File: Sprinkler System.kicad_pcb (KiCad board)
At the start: 2 copper layers, 165 x 85 mm, 81 parts, among them J1 Main Supply, J2 XFMR_Out, J20 Station_0, J21 Station_1, J22 Station_2, J23 Station_3, J24 Station_4, J25 Station_5, J3 XFMR_In, J4 Conn_Button, J5 UART0, J6 I2C, K1 G3MB-202P, K20 G5LE-1-DC5, K21 G5LE-1-DC5, K22 G5LE-1-DC5, K23 G5LE-1-DC5, K24 G5LE-1-DC5, K25 G5LE-1-DC5, SW1 EN, SW2 BOOT, U1 AMS1117-3.3, U2 EL817, U3 HLK-PM01, U4 ESP32-WROOM-32U, U5 ULN2803A

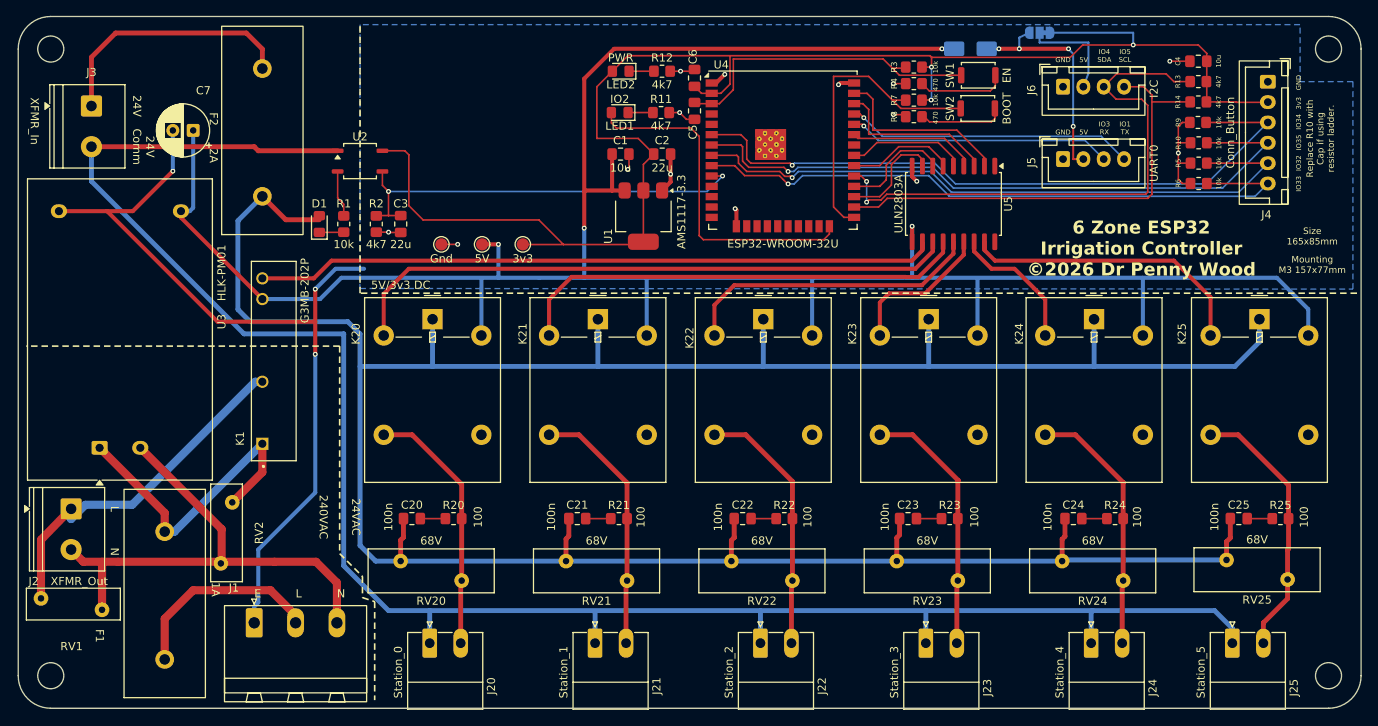
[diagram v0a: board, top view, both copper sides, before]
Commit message: Revise board: renumber parts, drop D2, J1 to Phoenix PT 5.0mm
Hand-edited layout changes plus regenerated fabrication outputs:
- Renumber C/R references (EN reset now C6, +5V bulk 220uF now C5,
  ESP32 VDD decoupling C4, +3V3 10uF C7; button pull-downs R5/R8/R10/R11)
- Remove D2 Schottky; J5 pin 2 (UART 5V) now ties directly to +5V
- Replace J1 with Phoenix PT 1,5/3-5.0 (5.0mm, mains-rated) terminal block
- Swap RV1/RV2 roles: RV1 across mains L-N input, RV2 across SSR output
  / transformer primary; RV footprints to stock D12mm_W4mm
- Regenerate gerbers, drill, POS, BOM, netlist, and PDFs to match

Co-Authored-By: Claude Opus 4.8 <noreply@anthropic.com>
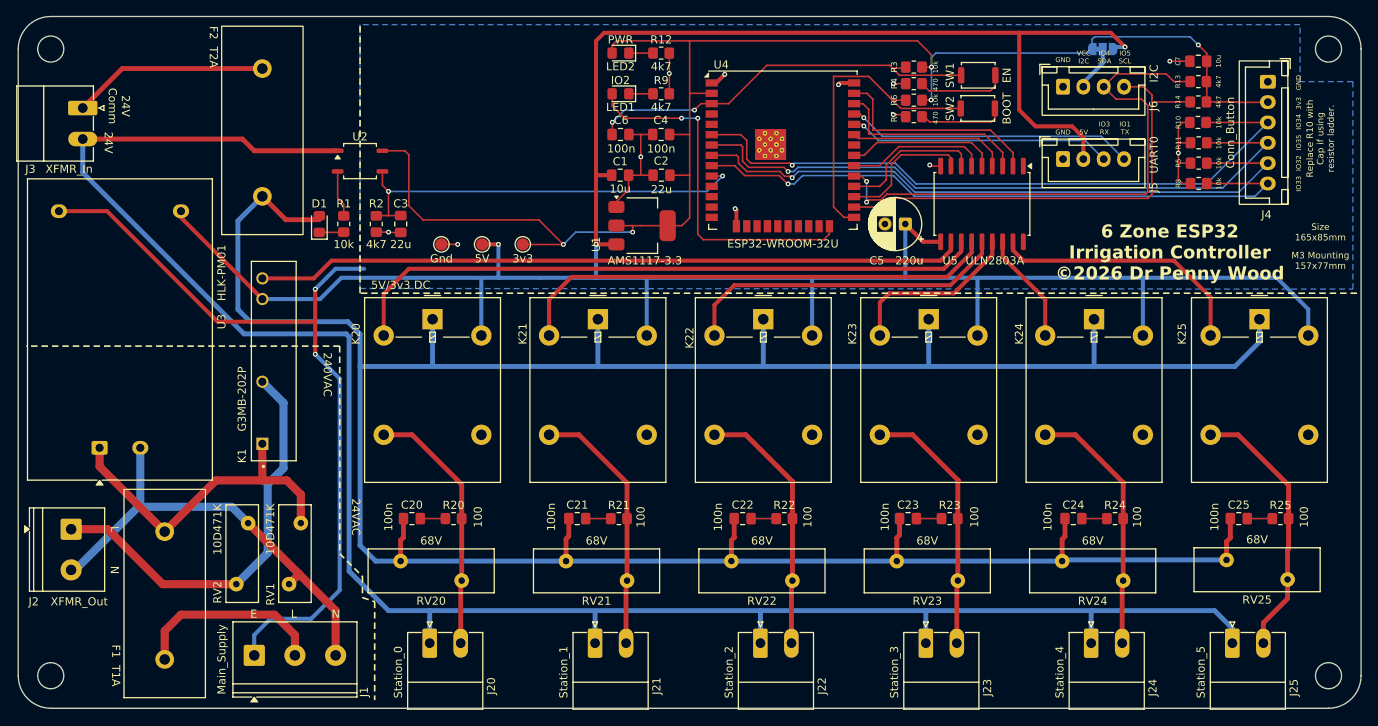
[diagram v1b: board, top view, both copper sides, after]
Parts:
- removed the C5 at (136.1, 57.6)
- removed D2: SS34, D_SMA
- added C4: 100n, Capacitor_SMD:C_0805_2012Metric_Pad1.18x1.45mm_HandSolder, F.Cu at (132.0, 60.5)
- F1: value 1A -> T1A
- F2: value 2A -> T2A
- J1: value Main Supply -> Main_Supply; footprint Sprinkler System:PhoenixContact_MSTBA_2,5_3-G-5,08_1x03_P5.08mm_Horizontal_EdgeClip -> TerminalBlock_Phoenix:TerminalBlock_Phoenix_PT-1,5-3-5.0-H_1x03_P5.00mm_Horizontal
- J3: footprint TerminalBlock_Phoenix:TerminalBlock_Phoenix_PT-1,5-2-5.0-H_1x02_P5.00mm_Horizontal -> Connector_Phoenix_MC:PhoenixContact_MC_1,5_2-G-3.81_1x02_P3.81mm_Horizontal
- JP1: footprint SolderJumper-3_P1.3mm_Bridged12_RoundedPad1.0x1.5mm_NumberLabels -> Jumper:SolderJumper-3_P1.3mm_Bridged12_RoundedPad1.0x1.5mm_NumberLabels
- RV1: renamed from RV2; footprint Varistor:RV_Disc_D12mm_W3.9mm_P7.5mm -> Varistor:RV_Disc_D12mm_W4mm_P7.5mm
- RV2: renamed from RV1; footprint Sprinkler System:RV_Disc_D12mm_W3.9mm_P7.5mm_EdgeClip -> Varistor:RV_Disc_D12mm_W4mm_P7.5mm
- moved C5 88.3 mm to (162.0, 71.5)
- moved RV2 24.1 mm to (79.8, 115.8), turned to 90 degrees
- moved C6 11.5 mm to (127.0, 60.5), turned to 180 degrees
- moved RV1 8.80 mm to (87.7, 108.2)
- moved JP1 8.00 mm to (186.2, 50.0), turned to 0 degrees
- moved J1 4.00 mm to (82.0, 124.5)
- moved U5 3.51 mm to (171.4, 69.0)
- moved C2 2.59 mm to (132.0, 65.5), turned to 180 degrees
- moved C1 2.59 mm to (127.0, 65.5)
- moved J2 2.50 mm to (59.5, 109.0)
- moved LED1 2.31 mm to (127.0, 55.5)
- moved R9 2.31 mm to (132.0, 55.5)
- moved R12 2.23 mm to (132.0, 50.5)
- moved LED2 2.23 mm to (127.0, 50.5)
- moved U1 1.18 mm to (129.7, 71.7), turned to 0 degrees
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- renumbered C7 to C5, C4 to C7, R9 to R10, R10 to R11, R7 to R6, R8 to R7, R6 to R8, R11 to R9
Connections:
- net /J6_VCC renamed /VCC_I2C
- C6 pad 1: +3V3 -> GND
- C6 pad 2: GND -> /EN
- J5 pad 2: /+5V_UART -> +5V
- JP1 pad 3: /+5V_UART -> +5V
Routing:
- net +5V: track 291.1 -> 324.5 mm, vias 4 -> 3
- net /+5V_UART: track 27.8 -> 0.00 mm, vias 4 -> 0
- net /EN: track 39.7 -> 49.4 mm, vias 0 -> 2
- net Neut: track 63.5 -> 55.5 mm
- net 24V_Supply: track 31.4 -> 24.1 mm
- net L_SW: track 44.2 -> 51.4 mm
- net /VCC_I2C: track 12.7 -> 5.61 mm
- net +3V3: track 190.6 -> 185.4 mm, vias 3 -> 5
- net /Zone0: track 13.7 -> 17.7 mm
- net /Zone1: track 13.3 -> 17.3 mm
- net /Zone4: track 20.2 -> 24.2 mm
- net /Zone3: track 15.7 -> 19.6 mm
- net /Zone5: track 22.6 -> 26.4 mm
- net /Zone2: track 14.7 -> 18.5 mm
- net /24V_On: track 13.0 -> 16.7 mm
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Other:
- board text added: "M3 Mounting 157x77mm"
- board text added: "VCC I2C"
- board text removed: "D2: SS34 or bridge"
- board text removed: "Mounting M3 157x77mm"
